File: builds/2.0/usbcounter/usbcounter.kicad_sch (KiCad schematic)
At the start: 39 parts

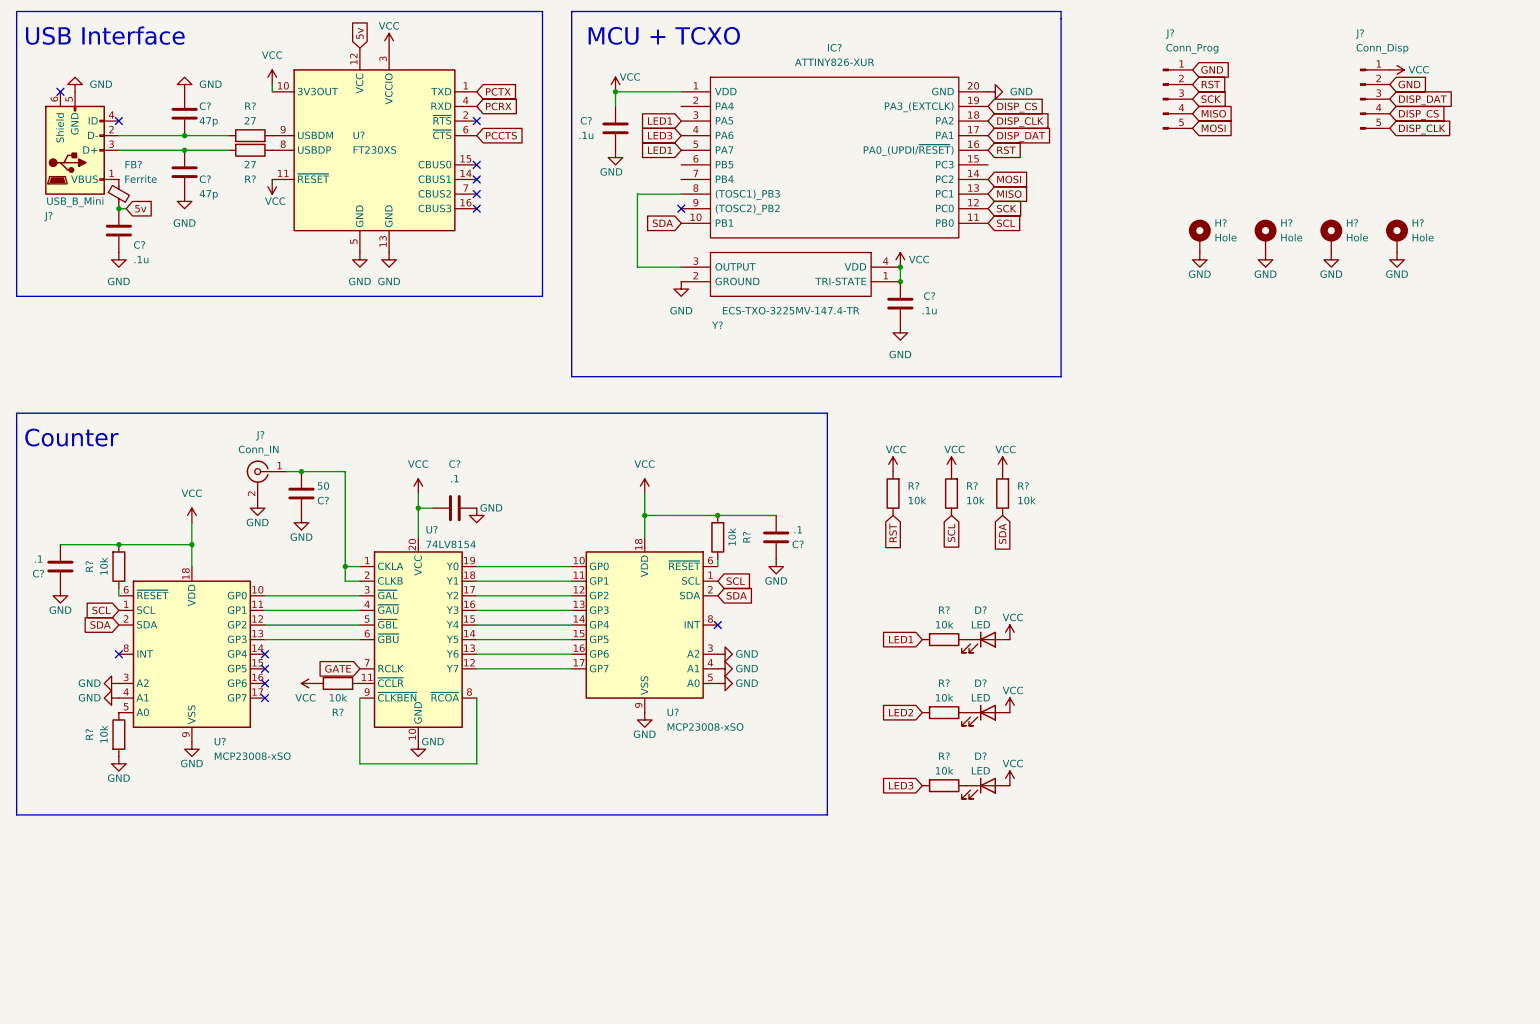
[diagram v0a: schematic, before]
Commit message: USB Counter 2.0: add 3.3v regulator
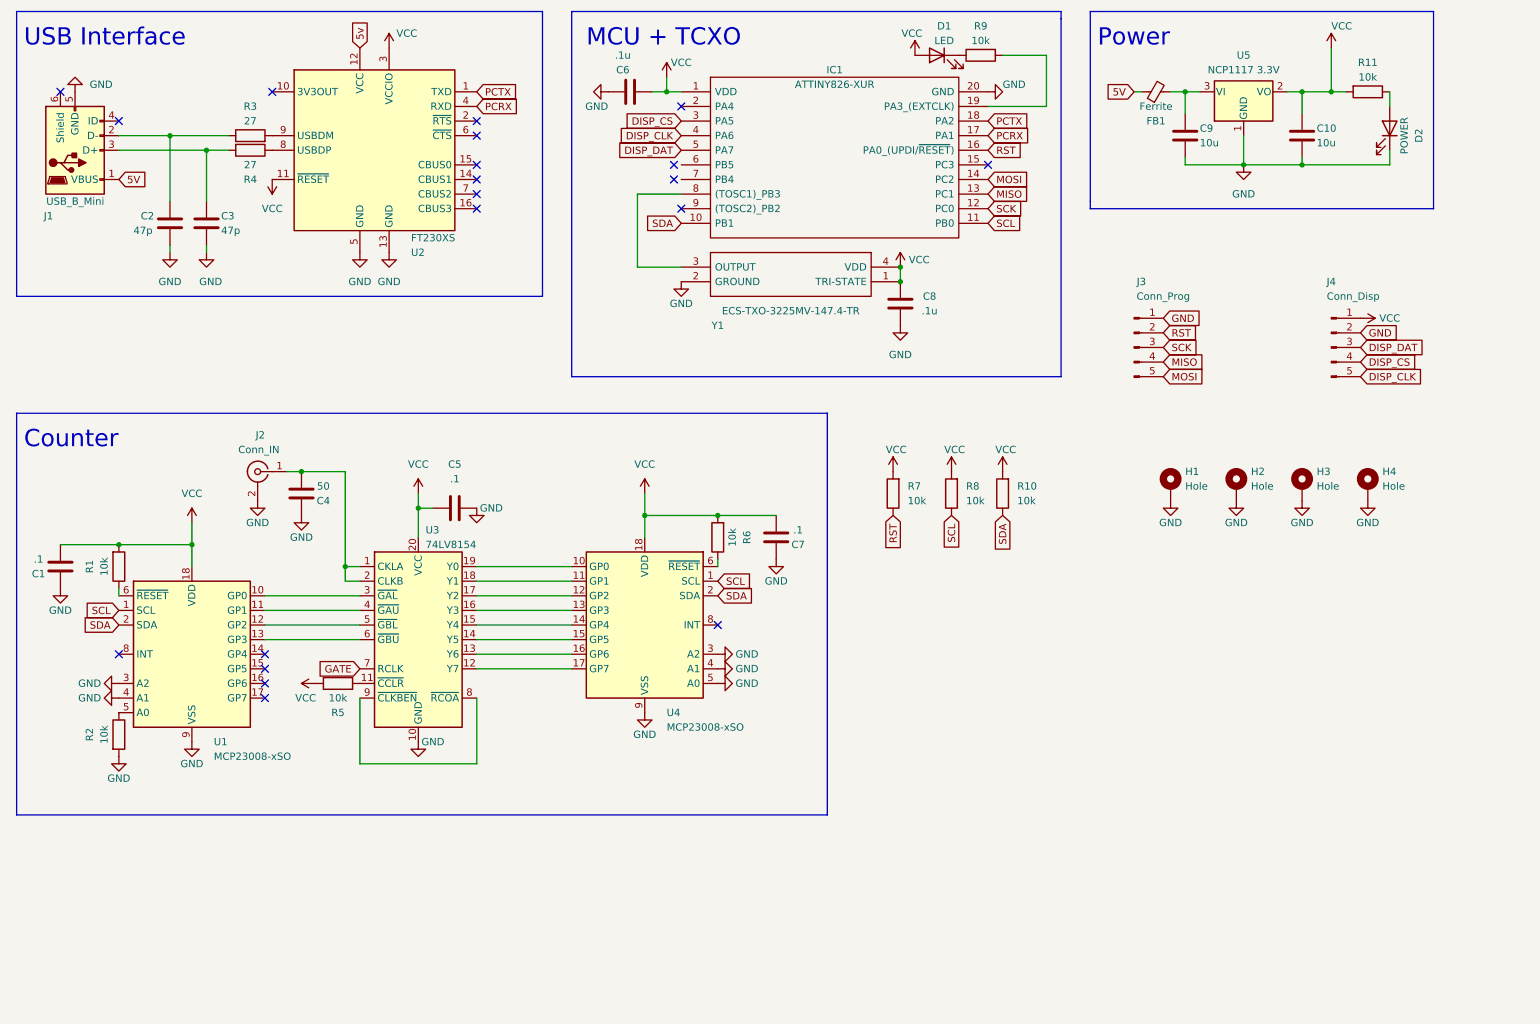
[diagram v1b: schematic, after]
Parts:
- removed C? (x2): 47p, symbol Device:C
- removed C?: .1u, symbol Device:C
- removed D? (x3): LED, symbol Device:LED
- removed FB?: Ferrite, symbol Device:FerriteBead_Small
- removed H? (x4): Hole, symbol Mechanical:MountingHole_Pad
- removed J?: USB_B_Mini, symbol Connector:USB_B_Mini
- removed J?: Conn_Prog, symbol Connector:Conn_01x05_Male
- removed J?: Conn_Disp, symbol Connector:Conn_01x05_Male
- removed R? (x2): 27, symbol Device:R
- removed R? (x3): 10k, symbol Device:R
- removed U?: FT230XS, Package_SO:SSOP-16_3.9x4.9mm_P0.635mm, symbol Interface_USB:FT230XS
- added C10, C9: 10u, symbol Device:C
- added C2, C3: 47p, symbol Device:C
- added D1: LED, symbol Device:LED
- added D2: POWER, symbol Device:LED
- added FB1: Ferrite, symbol Device:FerriteBead_Small
- added H1, H2, H3, H4: Hole, symbol Mechanical:MountingHole_Pad
- added J1: USB_B_Mini, symbol Connector:USB_B_Mini
- added J3: Conn_Prog, symbol Connector:Conn_01x05_Male
- added J4: Conn_Disp, symbol Connector:Conn_01x05_Male
- added R11, R9: 10k, symbol Device:R
- added R3, R4: 27, symbol Device:R
- added U2: FT230XS, Package_SO:SSOP-16_3.9x4.9mm_P0.635mm, symbol Interface_USB:FT230XS
- added U5: NCP1117 3.3V, Package_TO_SOT_SMD:SOT-223-3_TabPin2, symbol Regulator_Linear:NCP1117-3.3_SOT223
- gave numbers to parts that had none: 19
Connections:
- net LED3 is gone; now on net DISP_CLK: IC1.4 (PA6)
- net 5v: now also U2.12 (VCC)
- net DISP_CLK: now also J4.5 (Pin_5); no longer IC1.18 (PA2)
- net DISP_CS: now also IC1.3 (PA5), J4.4 (Pin_4); no longer IC1.19 (PA3_(EXTCLK))
- net DISP_DAT: now also IC1.5 (PA7), J4.3 (Pin_3); no longer IC1.17 (PA1)
- net GND: now also C10.2, C2.1, C3.1, C9.2, D2.1 (K), H1.1, H2.1, H3.1, H4.1, J1.5 (GND), J3.1 (Pin_1), J4.2 (Pin_2), U2.13 (GND), U2.5 (GND), U5.1 (GND)
- net MISO: now also J3.4 (Pin_4)
- net MOSI: now also J3.5 (Pin_5)
- net PCRX: now also IC1.17 (PA1), U2.4 (RXD)
- net PCTX: now also IC1.18 (PA2), U2.1 (TXD)
- net RST: now also J3.2 (Pin_2)
- net SCK: now also J3.3 (Pin_3)
- net VCC: now also C10.1, D1.2 (A), J4.1 (Pin_1), R11.2, U2.11 (~{RESET}), U2.3 (VCCIO), U5.2 (VO)
- removed net LED1: IC1.3 (PA5), IC1.5 (PA7)
- new net: C2.2, J1.2 (D-), R3.1
- new net: R3.2, U2.9 (USBDM)
- new net: C9.1, FB1.2, U5.3 (VI)
- new net: D1.1 (K), R9.1
- new net: R4.1, U2.8 (USBDP)
- new net: IC1.19 (PA3_(EXTCLK)), R9.2
- new net: D2.2 (A), R11.1
- new net: C3.2, J1.3 (D+), R4.2
- new net 5V: FB1.1, J1.1 (VBUS)
- no-connect marks 14 -> 20
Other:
- note added: "Power"
- moved on the sheet: C6

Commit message: 2.0: improve wiring
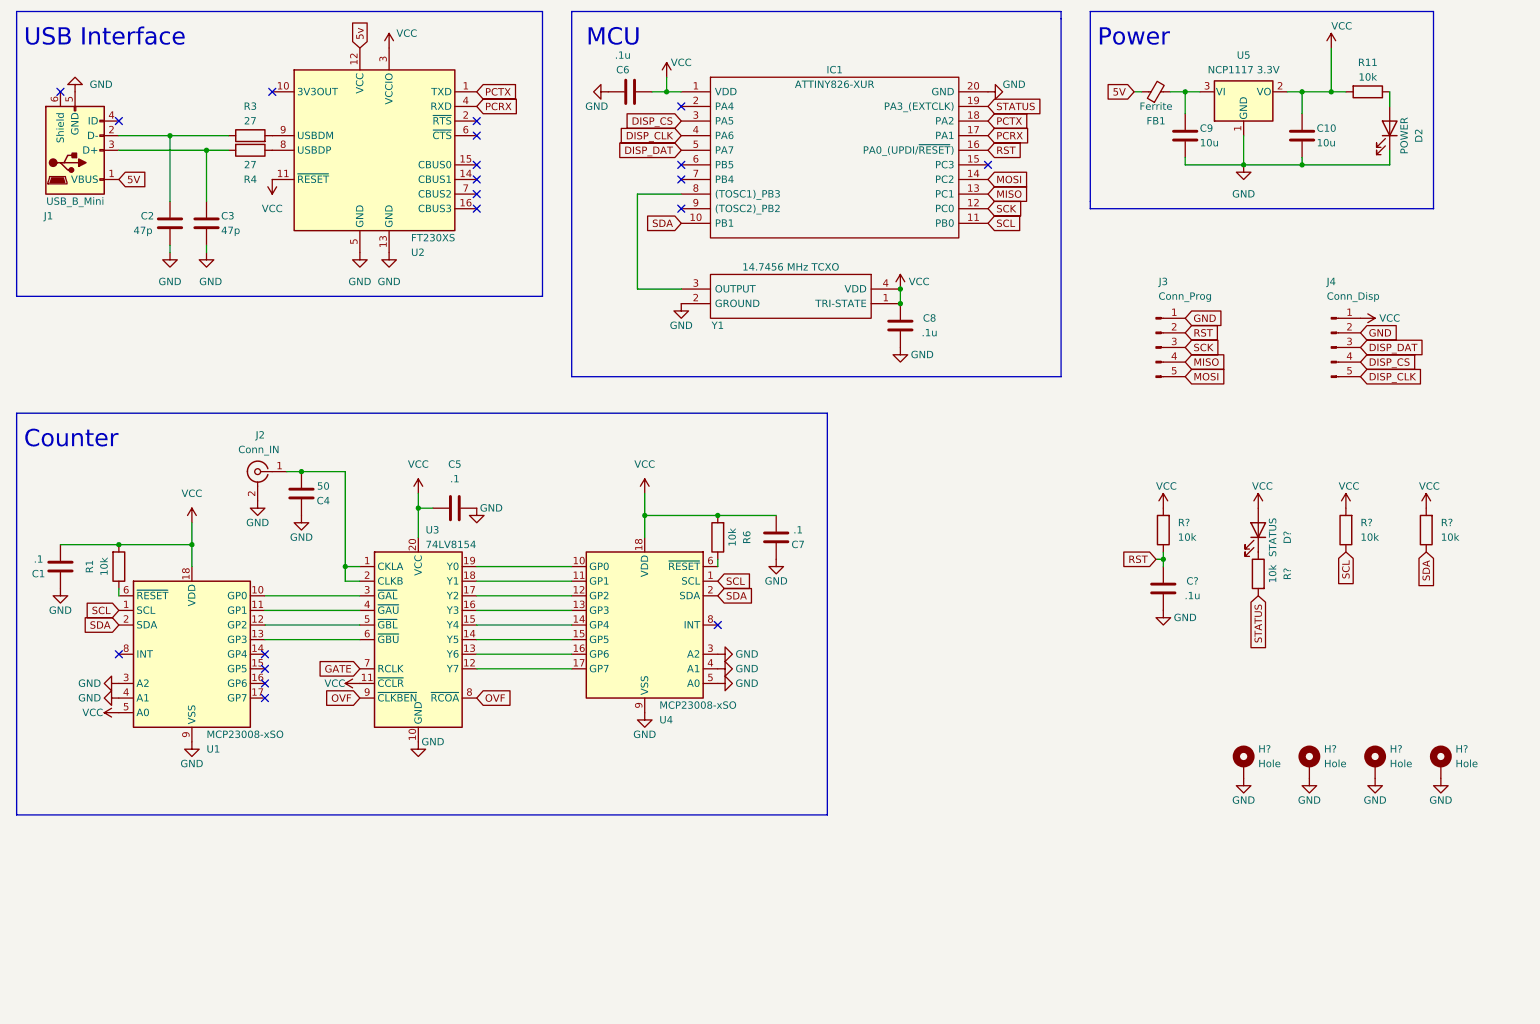
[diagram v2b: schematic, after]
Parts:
- removed D1: LED, symbol Device:LED
- removed H1, H2, H3, H4: Hole, symbol Mechanical:MountingHole_Pad
- removed R10, R2, R5, R7, R8, R9: 10k, symbol Device:R
- added C?: .1u, symbol Device:C
- added D?: STATUS, symbol Device:LED
- added H? (x4): Hole, symbol Mechanical:MountingHole_Pad
- added R? (x4): 10k, symbol Device:R
- Y1: value ECS-TXO-3225MV-147.4-TR -> 14.7456 MHz TCXO
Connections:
- net GND: now also C?.2, H?.1, H?.1, H?.1, H?.1
- net RST: now also C?.1, R?.1
- net SCL: now also R?.1
- net SDA: now also R?.1
- net VCC: now also U1.5 (A0), U3.11 (~{CCLR}), D?.2 (A), R?.2, R?.2, R?.2
- net OVF: now reaches U3.8 (~{RCOA}), U3.9 (~{CLKBEN})
- net STATUS: now reaches IC1.19 (PA3_(EXTCLK))
- net STATUS: now also R?.2
- new net: D?.1 (K), R?.1
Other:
- note added: "MCU"
- note removed: "MCU + TCXO"
- moved on the sheet: C8, J3, Y1

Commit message: 3.0: improve annotations
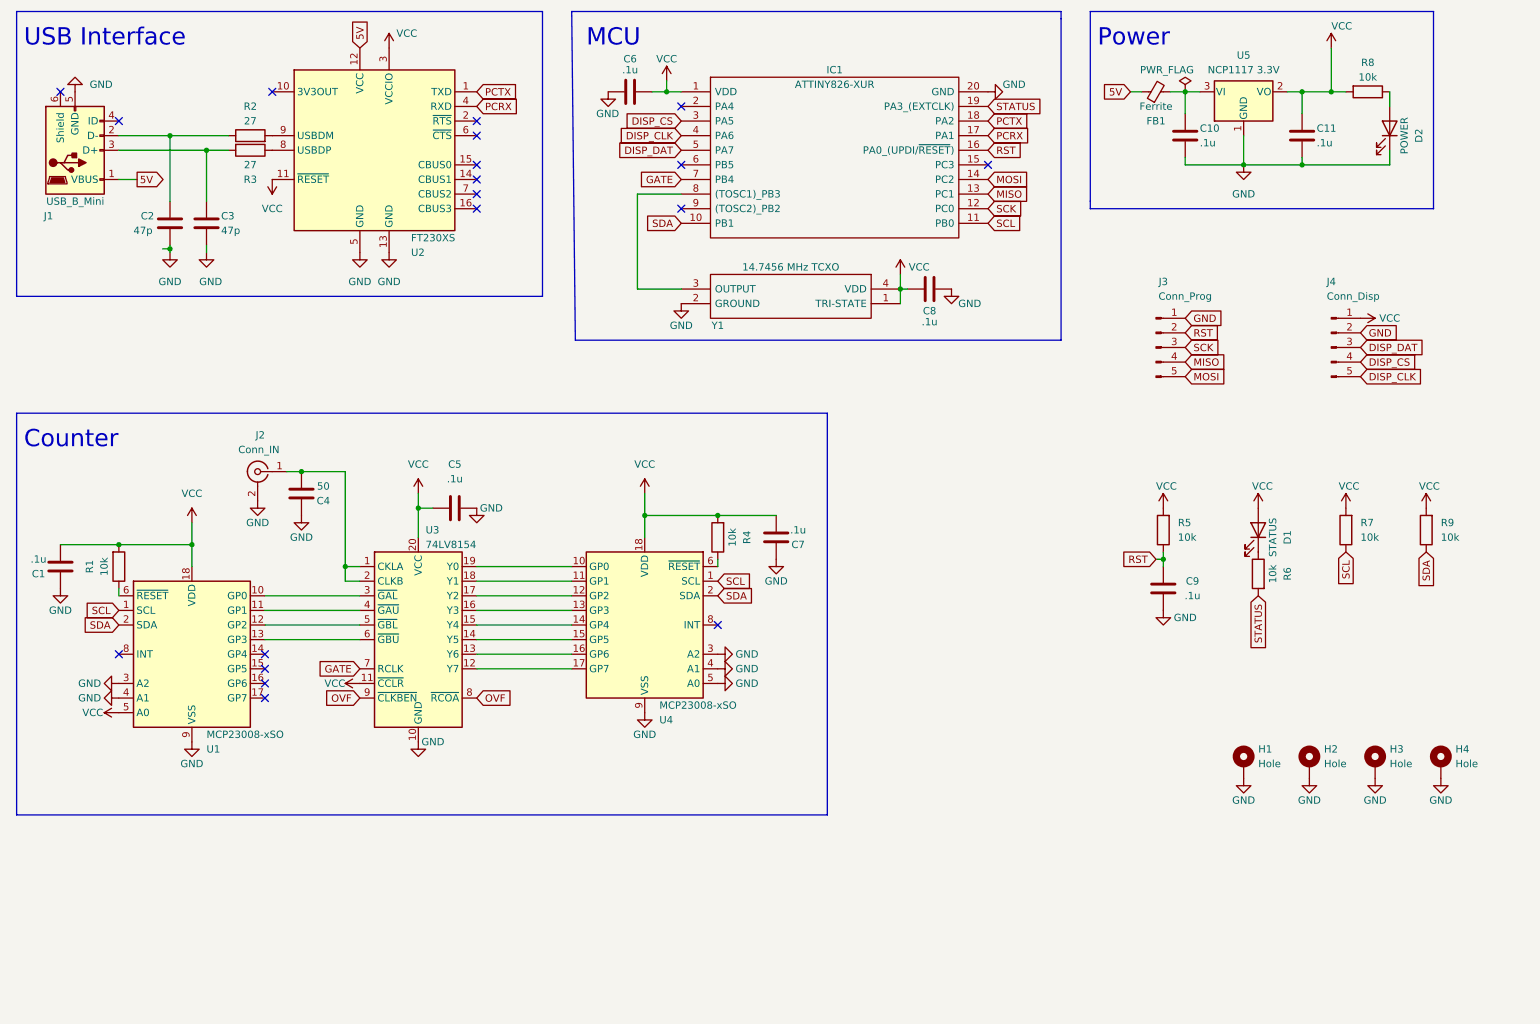
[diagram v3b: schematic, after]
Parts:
- C1, C5, C7: value .1 -> .1u
- C10: renamed from C9; value 10u -> .1u
- C11: renamed from C10; value 10u -> .1u
- IC1: footprint SOP65P780X200-20N -> Library Loader:SOP65P780X200-20N
- Y1: footprint ECSTXO3225MV1474TR -> Library Loader:ECSTXO3225MV1474TR
- gave numbers to parts that had none: 10
- renumbered R3 to R2, R4 to R3, R6 to R4, R11 to R8
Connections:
- net 5v is gone; now on net 5V: U2.12 (VCC)
- net GATE: now also IC1.7 (PB4)
- net GND: now also C8.1; no longer C8.2
- net VCC: now also C8.2; no longer C8.1
- no-connect marks 20 -> 19
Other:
- moved on the sheet: C8

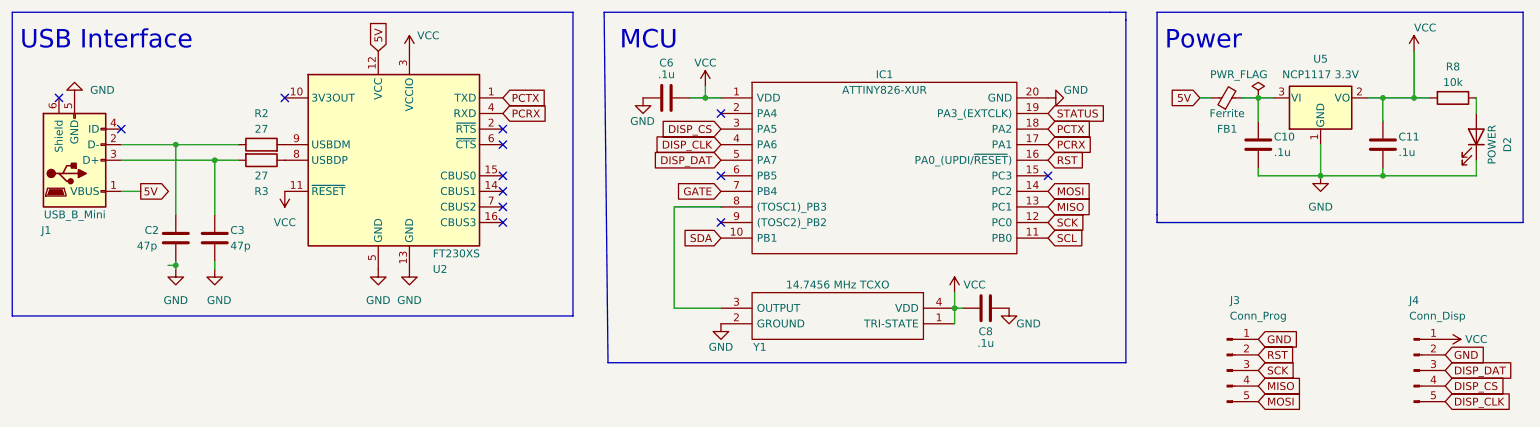
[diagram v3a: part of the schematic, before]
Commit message: 3.0: assign footprints
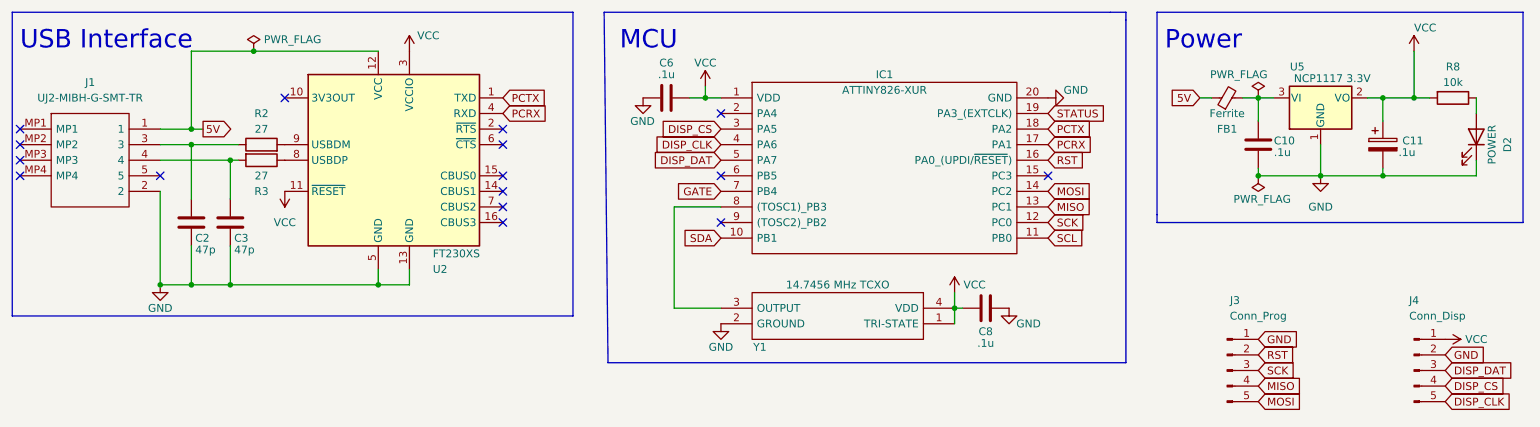
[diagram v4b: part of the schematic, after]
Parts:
- removed C11: .1u, symbol Device:C
- removed J1: USB_B_Mini, symbol Connector:USB_B_Mini
- added C11: .1u, Capacitor_Tantalum_SMD:CP_EIA-2012-15_AVX-P_Pad1.30x1.05mm_HandSolder, symbol Device:C_Polarized
- added J1: UJ2-MIBH-G-SMT-TR, Library Loader:UJ2MIBHGSMTTR, symbol Library Loader:UJ2-MIBH-G-SMT-TR
- C1, C10, C2, C3, C4, C5, C6, C7, C8, C9: footprint (none) -> Capacitor_SMD:C_0805_2012Metric_Pad1.18x1.45mm_HandSolder
- D1, D2: footprint (none) -> LED_SMD:LED_0805_2012Metric_Pad1.15x1.40mm_HandSolder
- FB1: footprint (none) -> Inductor_SMD:L_0805_2012Metric_Pad1.15x1.40mm_HandSolder
- H1, H2, H3, H4: footprint (none) -> MountingHole:MountingHole_2.2mm_M2_DIN965_Pad
- J2: footprint (none) -> Connector_Coaxial:SMA_Amphenol_132291_Vertical
- J3, J4, R1, R2, R3, R4, R5, R6, R7, R8, R9: footprint (none) -> Resistor_SMD:R_0805_2012Metric_Pad1.20x1.40mm_HandSolder
- U3: footprint (none) -> Package_SO:TSSOP-20_4.4x6.5mm_P0.65mm
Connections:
- net 5V: now also J1.1
- net GND: now also C11.2, J1.2
- net VCC: now also C11.1
- net at C2.2, R2.1: now also J1.3
- net at C3.2, R3.2: now also J1.4
- no-connect marks 19 -> 22
